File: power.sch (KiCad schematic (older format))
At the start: 0 parts

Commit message: Add MIC29302 LDO, VBAT will be used instead of 3.3V in order to reduce power consumption.
When testing this will require a ~3.8V supply at the M.2 connector!
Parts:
- added C? (x2): CP1, symbol CP1
- added C? (x2): C, symbol C
- added R?: 100k, symbol R
- added R?: 47k, symbol R
- added U?: MIC29302, symbol MIC29302
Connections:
- new net: R?.1, R?.2, U?.5 (ADJ)
- new net GND: C?.2, C?.2, C?.2, C?.2, R?.2, U?.3 (GND), U?.6 (GND)
- new net Vin: C?.1, C?.1, U?.2 (Vin)
- new net Vout: C?.1, C?.1, R?.1, U?.4 (Vout)
- new net ~Power_Off: U?.1 (EN)
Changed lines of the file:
@@
 Comment4 ""
 $EndDescr
+$Comp
+L MIC29302 U?
+U 1 1 5AB1921F
+P 5550 3600
+F 0 "U?" H 5200 3850 60  0000 C CNN
+F 1 "MIC29302" H 5750 3850 60  0000 C CNN
+F 2 "" H 5800 3550 60  0000 C CNN
+F 3 "" H 5800 3550 60  0000 C CNN
+	1    5550 3600
+	1    0    0    -1
+$EndComp
+$Comp
+L GND #PWR?
+U 1 1 5AB193E7
+P 5550 4050
+F 0 "#PWR?" H 5550 3800 50  0001 C CNN
+F 1 "GND" H 5550 3900 50  0000 C CNN
+F 2 "" H 5550 4050 50  0001 C CNN
+F 3 "" H 5550 4050 50  0001 C CNN
+	1    5550 4050
+	1    0    0    -1
+$EndComp
+$Comp
+L CP1 C?
+U 1 1 5AB19412
+P 4050 3700
+F 0 "C?" H 4075 3800 50  0000 L CNN
+F 1 "CP1" H 4075 3600 50  0000 L CNN
+F 2 "" H 4050 3700 50  0001 C CNN
+F 3 "" H 4050 3700 50  0001 C CNN
+	1    4050 3700
+	-1   0    0    -1
+$EndComp
+$Comp
+L C C?
+U 1 1 5AB19443
+P 4250 3700
+F 0 "C?" H 4275 3800 50  0000 L CNN
+F 1 "C" H 4275 3600 50  0000 L CNN
+F 2 "" H 4288 3550 50  0001 C CNN
+F 3 "" H 4250 3700 50  0001 C CNN
+	1    4250 3700
+	1    0    0    -1
+$EndComp
+$Comp
+L CP1 C?
+U 1 1 5AB194A7
+P 6700 3700
+F 0 "C?" H 6725 3800 50  0000 L CNN
+F 1 "CP1" H 6725 3600 50  0000 L CNN
+F 2 "" H 6700 3700 50  0001 C CNN
+F 3 "" H 6700 3700 50  0001 C CNN
+	1    6700 3700
+	-1   0    0    -1
+$EndComp
+$Comp
+L C C?
+U 1 1 5AB19573
+P 6900 3700
+F 0 "C?" H 6925 3800 50  0000 L CNN
+F 1 "C" H 6925 3600 50  0000 L CNN
+F 2 "" H 6938 3550 50  0001 C CNN
+F 3 "" H 6900 3700 50  0001 C CNN
+	1    6900 3700
+	1    0    0    -1
+$EndComp
+$Comp
+L R R?
+U 1 1 5AB195E5
+P 6250 3700
+F 0 "R?" H 6350 3750 50  0000 C CNN
+F 1 "100k" H 6400 3650 50  0000 C CNN
+F 2 "" V 6180 3700 50  0001 C CNN
+F 3 "" H 6250 3700 50  0001 C CNN
+	1    6250 3700
+	1    0    0    -1
+$EndComp
+$Comp
+L R R?
+U 1 1 5AB19636
+P 6250 4100
+F 0 "R?" H 6350 4150 50  0000 C CNN
+F 1 "47k" H 6400 4050 50  0000 C CNN
+F 2 "" V 6180 4100 50  0001 C CNN
+F 3 "" H 6250 4100 50  0001 C CNN
+	1    6250 4100
+	1    0    0    -1
+$EndComp
+$Comp
+L GND #PWR?
+U 1 1 5AB19681
+P 6250 4300
+F 0 "#PWR?" H 6250 4050 50  0001 C CNN
+F 1 "GND" H 6250 4150 50  0000 C CNN
+F 2 "" H 6250 4300 50  0001 C CNN
+F 3 "" H 6250 4300 50  0001 C CNN
+	1    6250 4300
+	1    0    0    -1
+$EndComp
+$Comp
+L GND #PWR?
+U 1 1 5AB198DF
+P 6700 3900
+F 0 "#PWR?" H 6700 3650 50  0001 C CNN
+F 1 "GND" H 6700 3750 50  0000 C CNN
+F 2 "" H 6700 3900 50  0001 C CNN
+F 3 "" H 6700 3900 50  0001 C CNN
+	1    6700 3900
+	1    0    0    -1
+$EndComp
+$Comp
+L GND #PWR?
+U 1 1 5AB1991A
+P 6900 3900
+F 0 "#PWR?" H 6900 3650 50  0001 C CNN
+F 1 "GND" H 6900 3750 50  0000 C CNN
+F 2 "" H 6900 3900 50  0001 C CNN
+F 3 "" H 6900 3900 50  0001 C CNN
+	1    6900 3900
+	1    0    0    -1
+$EndComp
+$Comp
+L GND #PWR?
+U 1 1 5AB19B43
+P 4050 3900
+F 0 "#PWR?" H 4050 3650 50  0001 C CNN
+F 1 "GND" H 4050 3750 50  0000 C CNN
+F 2 "" H 4050 3900 50  0001 C CNN
+F 3 "" H 4050 3900 50  0001 C CNN
+	1    4050 3900
+	1    0    0    -1
+$EndComp
+$Comp
+L GND #PWR?
+U 1 1 5AB19B9E
+P 4250 3900
+F 0 "#PWR?" H 4250 3650 50  0001 C CNN
+F 1 "GND" H 4250 3750 50  0000 C CNN
+F 2 "" H 4250 3900 50  0001 C CNN
+F 3 "" H 4250 3900 50  0001 C CNN
+	1    4250 3900
+	1    0    0    -1
+$EndComp
+Text HLabel 4950 3650 0    60   Input ~ 0
+~Power_Off
+Text HLabel 4000 3500 0    60   Input ~ 0
+Vin
+Text HLabel 6950 3500 2    60   Output ~ 0
+Vout
+Wire Wire Line
+	5550 4050 5550 4000
+Wire Wire Line
+	6100 3650 6150 3650
+Wire Wire Line
+	6150 3650 6150 3900
+Wire Wire Line
+	6150 3900 6250 3900
+Wire Wire Line
+	6250 3850 6250 3950
+Connection ~ 6250 3900
+Wire Wire Line
+	6250 4300 6250 4250
+Wire Wire Line
+	6100 3500 6950 3500
+Wire Wire Line
+	6700 3550 6700 3500
+Connection ~ 6700 3500
+Wire Wire Line
+	6700 3900 6700 3850
+Wire Wire Line
+	6900 3900 6900 3850
+Wire Wire Line
+	6250 3550 6250 3500
+Connection ~ 6250 3500
+Wire Wire Line
+	4000 3500 5000 3500
+Wire Wire Line
+	4050 3500 4050 3550
+Wire Wire Line
+	4250 3550 4250 3500
+Connection ~ 4250 3500
+Wire Wire Line
+	4050 3900 4050 3850
+Wire Wire Line
+	4250 3900 4250 3850
+Connection ~ 6900 3500
+Wire Wire Line
+	4950 3650 5000 3650
+Wire Wire Line
+	6900 3550 6900 3500
+Connection ~ 4050 3500
 $EndSCHEMATC

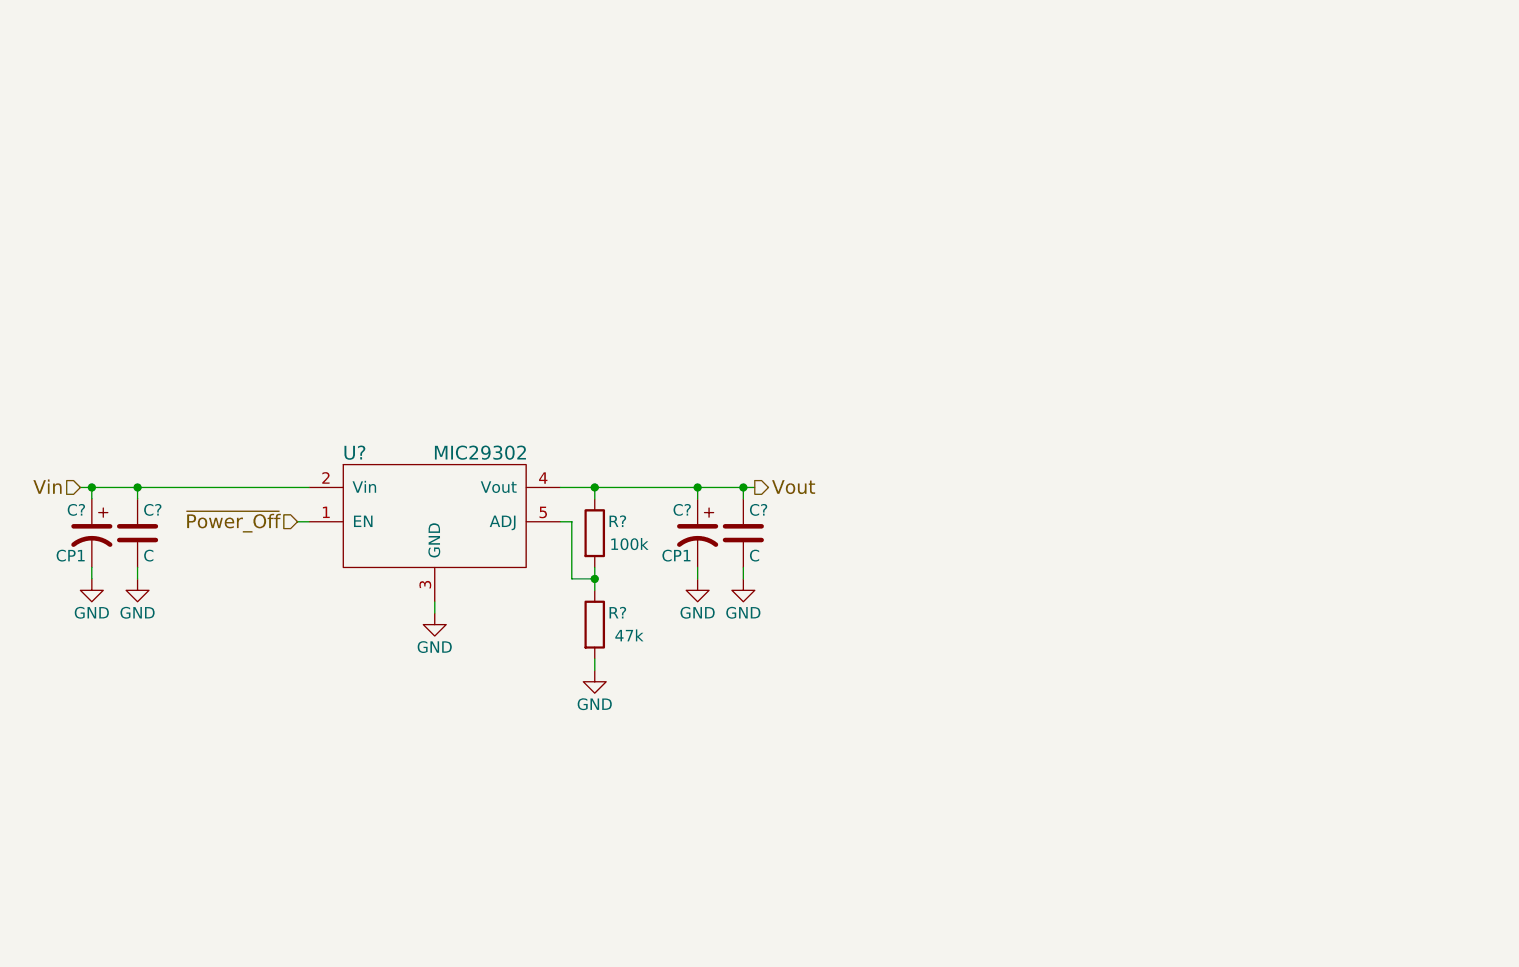
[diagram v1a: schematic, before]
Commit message: Selected which bulk capacitors will be used throughout the design, allowing for a small profile with high capacitance and fast transient response time (low ESR/ESL); also created the respective footprint
Put in a few notes regarding discrepancies between what the SIM7100 documentation suggests for cap values and what the MIC29302 datasheet says. I chose to go wivalues closer to what SIM7100 suggests but with a lower output cap value due to what photos of the mPCIe module shows. Namely, use of a few TMCUB0J107MTRF 100uF caps throughout the design, using this same cap near the regulator in place of an expensive 330uF one (as suggested in figure 9).
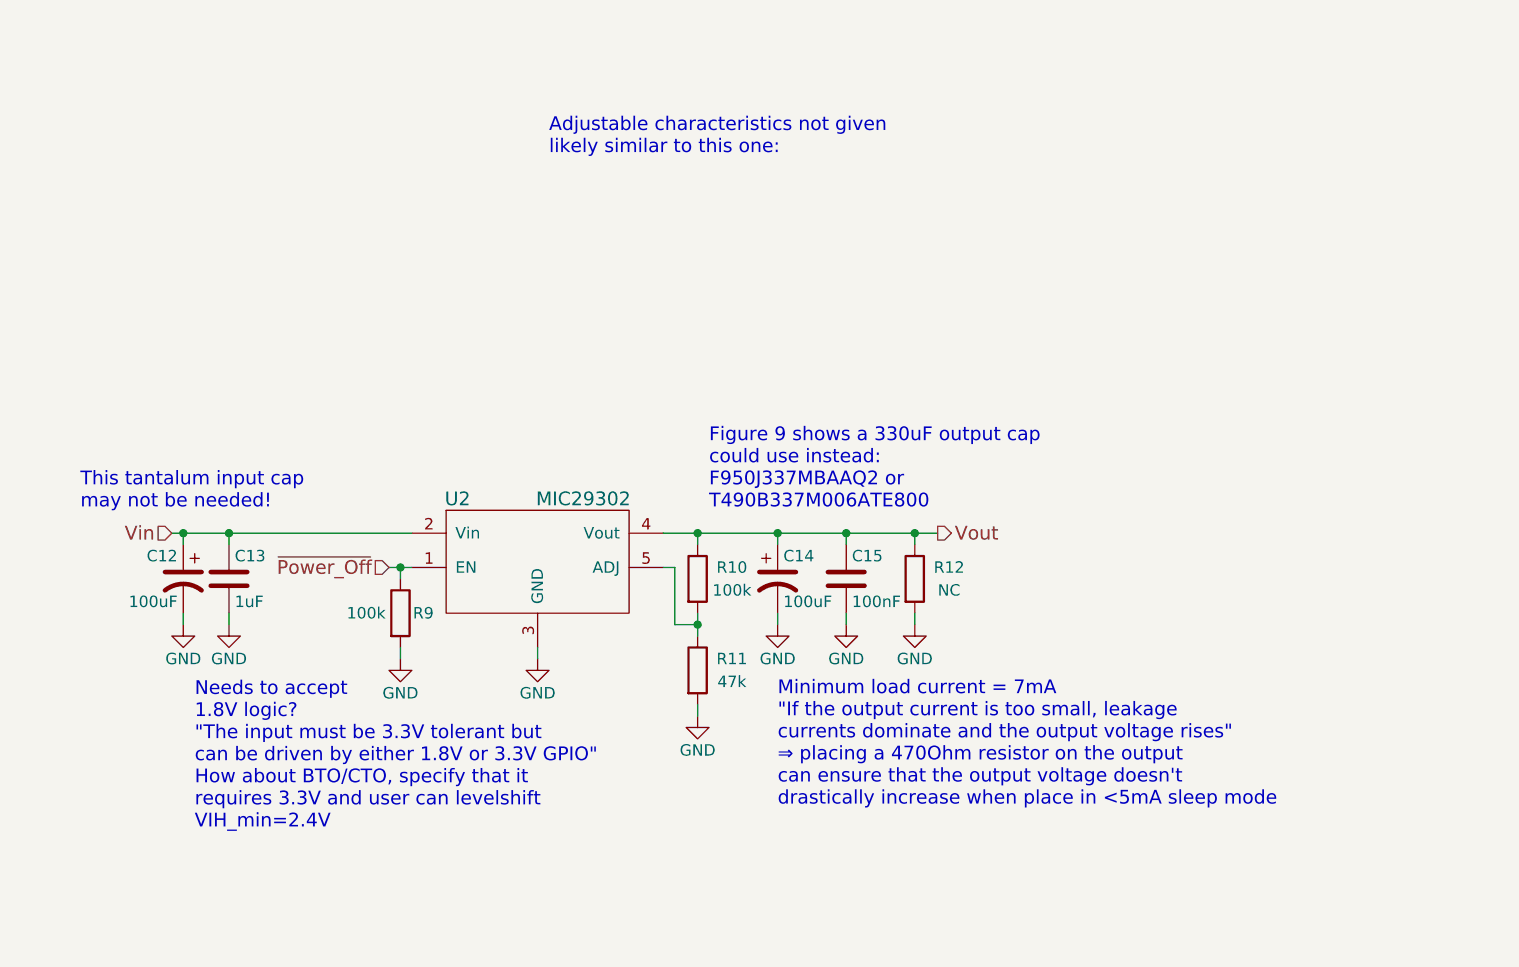
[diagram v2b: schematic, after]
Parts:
- added R12: NC, symbol R
- added R9: 100k, symbol R
- C12, C14: renamed from C?; value CP1 -> 100uF; footprint (none) -> m2_simcom_7100:CP_Tantalum_Case-B_EIA-3528-21_Reflow
- C13: renamed from C?; value C -> 1uF
- C15: renamed from C?; value C -> 100nF
- gave numbers to parts that had none: 3
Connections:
- net GND: now also R12.2, R9.2
- net Vout: now also R12.1
- net ~Power_Off: now also R9.1
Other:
- note added: "Adjustable characteristics not given\nlikely similar to this one:"
- note added: "Figure 9 shows a 330uF output cap\ncould use instead:\nF950J337MBAAQ2 or\nT490B337M006ATE800"
- note added: "Minimum load current = 7mA\n"If the output current is too small, leakage\ncurrents dominate and the output voltage rises"\n⇒ placing a 470Ohm resistor on the output\ncan ensure that the output voltage doesn't\ndrastically increase when place in <5mA sleep mode"
- note added: "Needs to accept\n1.8V logic?\n"The input must be 3.3V tolerant but\ncan be driven by either 1.8V or 3.3V GPIO"\nHow about BTO/CTO, specify that it\nrequires 3.3V and user can levelshift\nVIH_min=2.4V"
- note added: "This tantalum input cap\nmay not be needed!"
- moved on the sheet: C12, C13, C14, C15, R10, R11, U2

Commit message: Assign all footprints and generate netlist
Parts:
- C13, C15: footprint (none) -> Capacitors_SMD:C_0603
- R10, R11, R12, R9: footprint (none) -> Resistors_SMD:R_0603
- U2: footprint (none) -> m2_simcom_7100:TO-263-5_TabPin6
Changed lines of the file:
@@
 F 0 "U2" H 5650 4050 60  0000 C CNN
 F 1 "MIC29302" H 6200 4050 60  0000 C CNN
-F 2 "" H 6250 3750 60  0001 C CNN
+F 2 "m2_simcom_7100:TO-263-5_TabPin6" H 6250 3750 60  0001 C CNN
 F 3 "" H 6250 3750 60  0000 C CNN
 	1    6000 3800
@@
 F 0 "C13" H 4675 4000 50  0000 L CNN
 F 1 "1uF" H 4675 3800 50  0000 L CNN
-F 2 "" H 4688 3750 50  0001 C CNN
+F 2 "Capacitors_SMD:C_0603" H 4688 3750 50  0001 C CNN
 F 3 "" H 4650 3900 50  0001 C CNN
 	1    4650 3900
@@
 F 0 "R10" H 6850 3950 50  0000 C CNN
 F 1 "100k" H 6850 3850 50  0000 C CNN
-F 2 "" V 6630 3900 50  0001 C CNN
+F 2 "Resistors_SMD:R_0603" V 6630 3900 50  0001 C CNN
 F 3 "" H 6700 3900 50  0001 C CNN
 	1    6700 3900
@@
 F 0 "R11" H 6850 4350 50  0000 C CNN
 F 1 "47k" H 6850 4250 50  0000 C CNN
-F 2 "" V 6630 4300 50  0001 C CNN
+F 2 "Resistors_SMD:R_0603" V 6630 4300 50  0001 C CNN
 F 3 "" H 6700 4300 50  0001 C CNN
 	1    6700 4300
@@
 F 0 "R9" H 5500 4050 50  0000 C CNN
 F 1 "100k" H 5250 4050 50  0000 C CNN
-F 2 "" V 5330 4050 50  0001 C CNN
+F 2 "Resistors_SMD:R_0603" V 5330 4050 50  0001 C CNN
 F 3 "" H 5400 4050 50  0001 C CNN
 	1    5400 4050
@@
 F 0 "R12" H 7800 3950 50  0000 C CNN
 F 1 "NC" H 7800 3850 50  0000 C CNN
-F 2 "" V 7580 3900 50  0001 C CNN
+F 2 "Resistors_SMD:R_0603" V 7580 3900 50  0001 C CNN
 F 3 "" H 7650 3900 50  0001 C CNN
 	1    7650 3900
@@
 F 0 "C15" H 7375 4000 50  0000 L CNN
 F 1 "100nF" H 7375 3800 50  0000 L CNN
-F 2 "" H 7388 3750 50  0001 C CNN
+F 2 "Capacitors_SMD:C_0603" H 7388 3750 50  0001 C CNN
 F 3 "" H 7350 3900 50  0001 C CNN
 	1    7350 3900

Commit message: Swapping out the MIC29302 4.46mm thick TO-263 LDO with the smaller RT9059 WDFN-10L part which can handle the high current transients in a much more suitable package
The package is also much cheaper!
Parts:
- U2: value MIC29302 -> RT9059; footprint m2_simcom_7100:TO-263-5_TabPin6 -> (none)
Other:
- note added: "AP7176BFN-7 DFN drop-in\nMIC37303 closest DFN package to recommended"
- note removed: "Adjustable characteristics not given\nlikely similar to this one:"

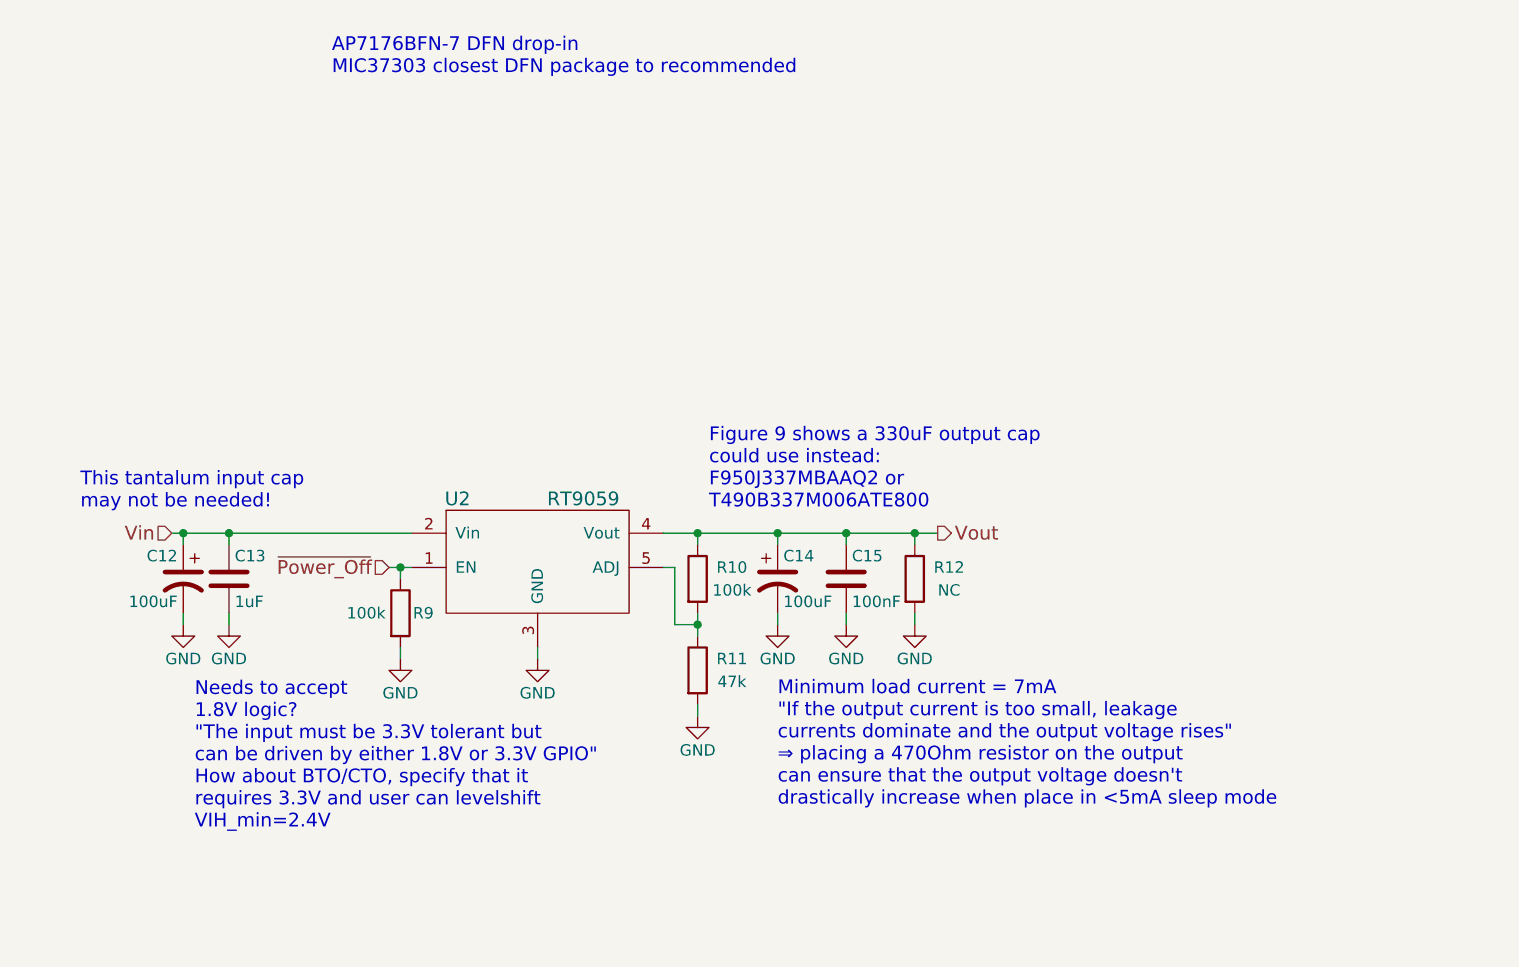
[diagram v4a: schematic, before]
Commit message: Use the RT9059 LDO in the layout instead of the old MIC29302 one
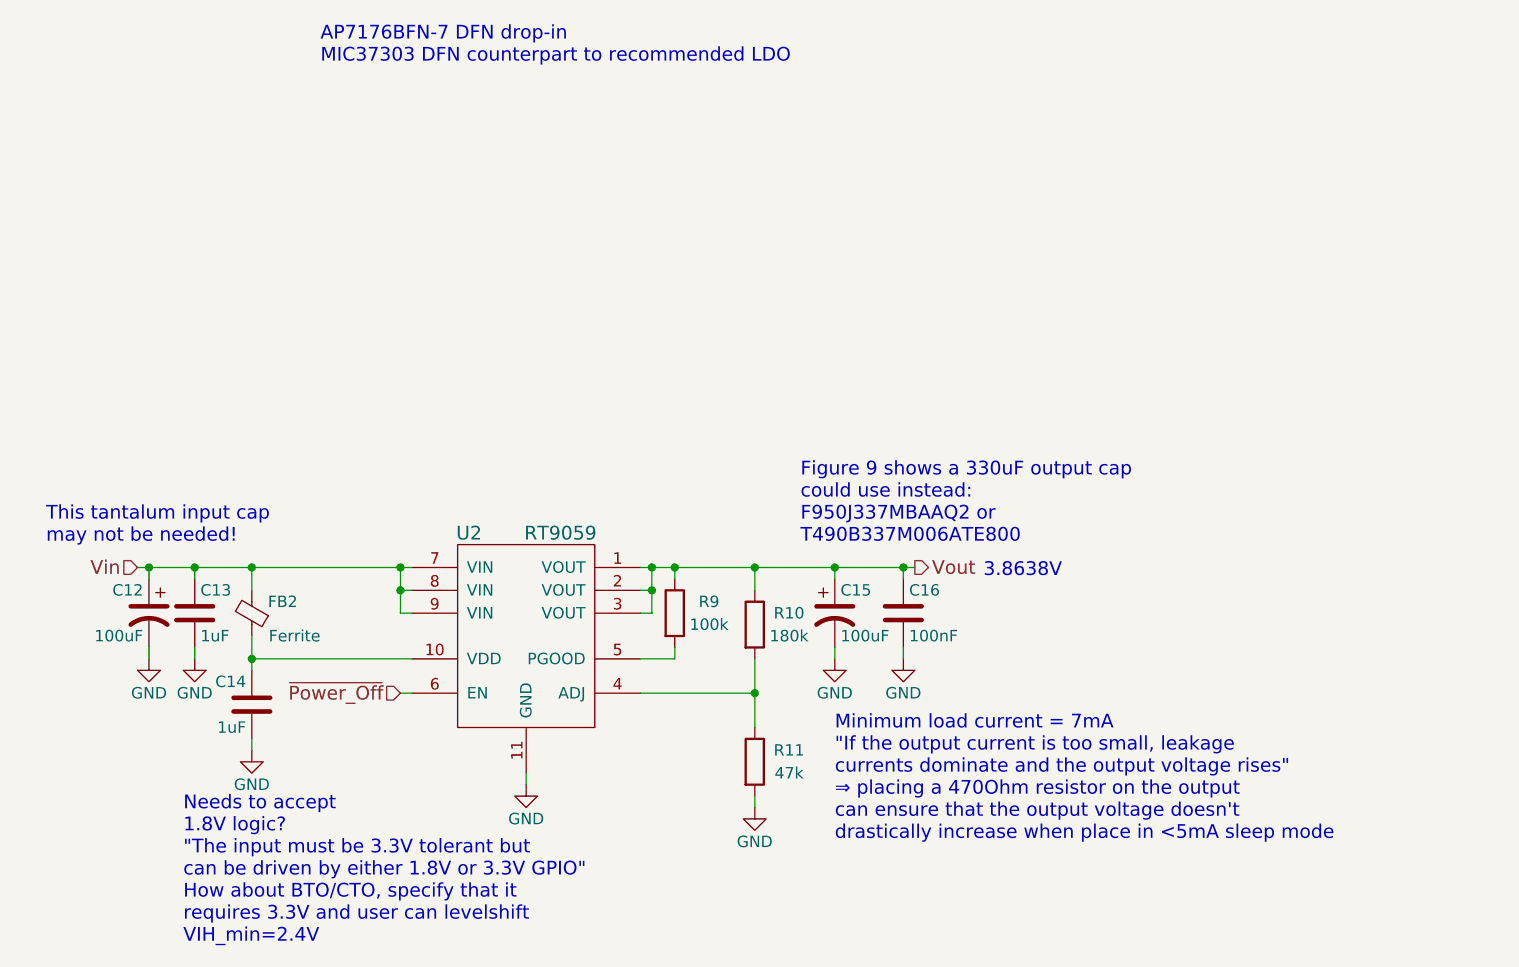
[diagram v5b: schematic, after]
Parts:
- removed R12: NC, Resistors_SMD:R_0603, symbol R
- removed U2: RT9059, symbol MIC29302
- added C14: 1uF, Capacitors_SMD:C_0603, symbol C
- added FB2: Ferrite, Inductors_SMD:L_0603, symbol Ferrite_Bead_Small
- added U2: RT9059, m2_simcom_7100:DFN-10-1EP_3x3mm_Pitch0.5mm, symbol RT9059
- R10: value 100k -> 180k
- renumbered C14 to C15, C15 to C16
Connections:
- net GND: now also C14.2, U2.11 (GND); no longer R9.2
- net Vin: now also FB2.2, U2.7 (VIN), U2.8 (VIN), U2.9 (VIN)
- net Vout: now also R9.1, U2.1 (VOUT), U2.2 (VOUT), U2.3 (VOUT)
- net ~Power_Off: now also U2.6 (EN); no longer R9.1
- net at R10.2, R11.1: now also U2.4 (ADJ)
- new net: C14.1, FB2.1, U2.10 (VDD)
- new net: R9.2, U2.5 (PGOOD)
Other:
- note added: "3.8638V"
- note added: "AP7176BFN-7 DFN drop-in\nMIC37303 DFN counterpart to recommended LDO"
- note removed: "AP7176BFN-7 DFN drop-in\nMIC37303 closest DFN package to recommended"
- moved on the sheet: C12, C13, C15, C16, R10, R11
